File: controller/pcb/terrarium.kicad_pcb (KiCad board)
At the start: 2 copper layers, 90 x 90 mm, 57 parts, among them Q1 S8050, Q2 S8050, Q3 S8050, SW1 RESET, SW2 BOOT, SW3 RESET RTC, U1 ESP32-WROOM-32, U2 DS3231M, U3 LM1117-3.3

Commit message: pcb: refactor
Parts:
- moved R2 0.51 mm to (107.0, 75.9)
- moved R4 0.51 mm to (89.0, 75.9)
- moved R6 0.51 mm to (71.0, 75.9)
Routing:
- net +3V3: track 186.9 -> 191.3 mm, vias 4 -> 5
- net G23: track 93.7 -> 90.7 mm, vias 4 -> 2
- net Net-(D4-Pad1): track 59.5 -> 56.7 mm, vias 0 -> 2
- net SCL: track 137.3 -> 138.9 mm, vias 5 -> 3
- net SDA: track 129.5 -> 130.5 mm, vias 4 -> 2

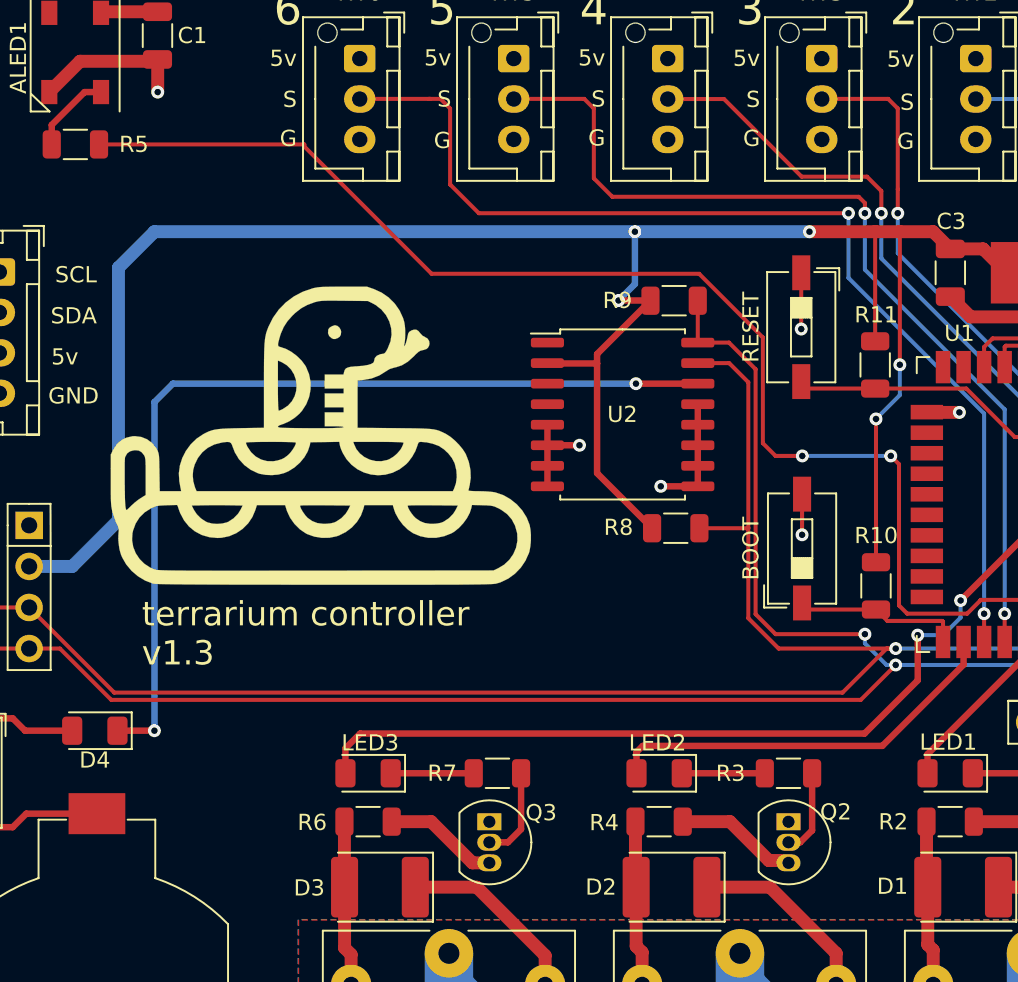
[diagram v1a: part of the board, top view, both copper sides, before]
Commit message: minor updates, bjt to sot-23
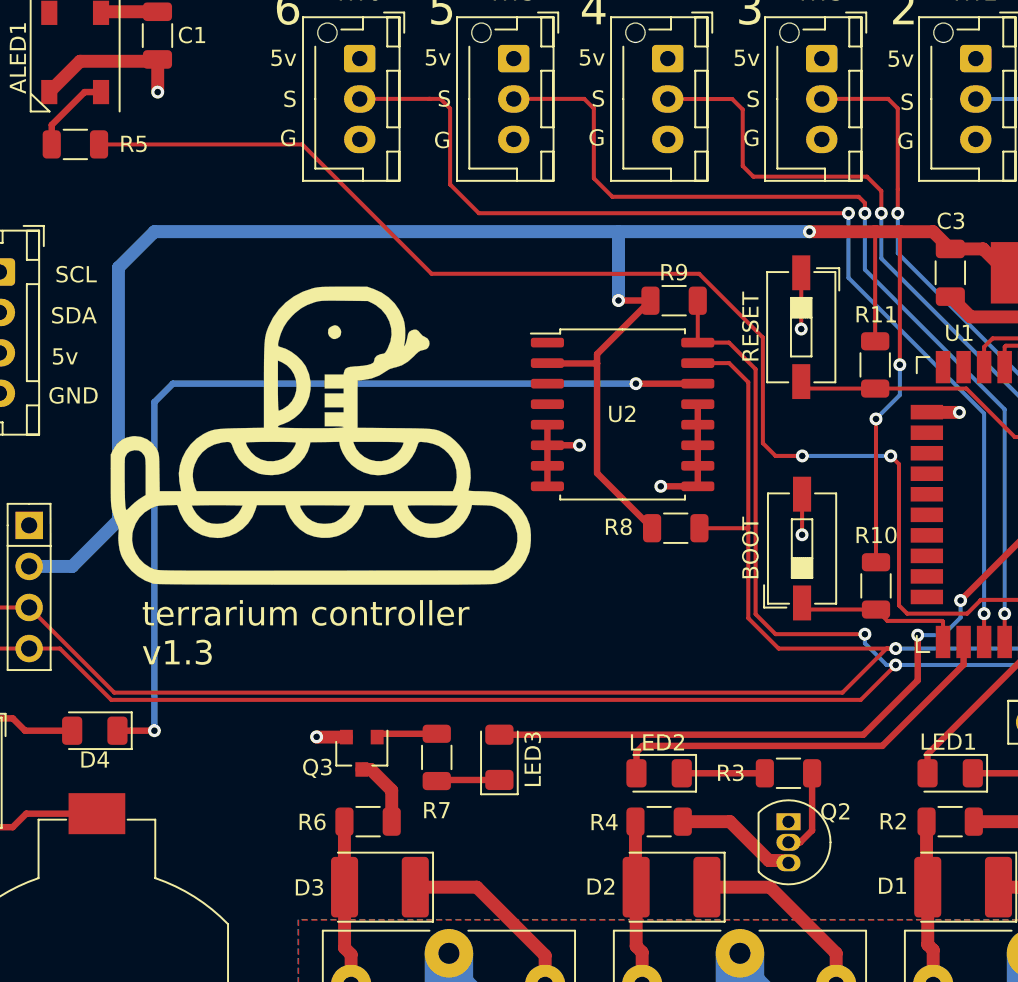
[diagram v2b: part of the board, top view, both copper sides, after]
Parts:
- Q3: footprint Package_TO_SOT_THT:TO-92_Inline -> Package_TO_SOT_SMD:SOT-23
- moved Q3 8.95 mm to (70.6, 71.6)
- moved LED3 8.18 mm to (79.1, 71.9), turned to 90 degrees
- moved R7 3.88 mm to (75.2, 71.9), turned to 90 degrees
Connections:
- Q3 pad 1: GND -> Net-(Q3-Pad1)
- Q3 pad 2: Net-(Q3-Pad2) -> GND
- R7 pad 2: Net-(Q3-Pad2) -> Net-(Q3-Pad1)
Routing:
- net G25: track 61.7 -> 50.3 mm
- net Net-(Q3-Pad2): track 5.76 -> 0.00 mm
- net Net-(Q3-Pad1): track 0.00 -> 3.77 mm
- net Net-(Q3-Pad3): track 7.26 -> 4.32 mm
- net G18: track 47.7 -> 49.7 mm
- net GND: track 79.4 -> 81.2 mm, vias 10 -> 11
- net Net-(LED3-Pad1): track 5.14 -> 3.90 mm
- net +3V3: track 191.3 -> 190.9 mm, vias 5 -> 4

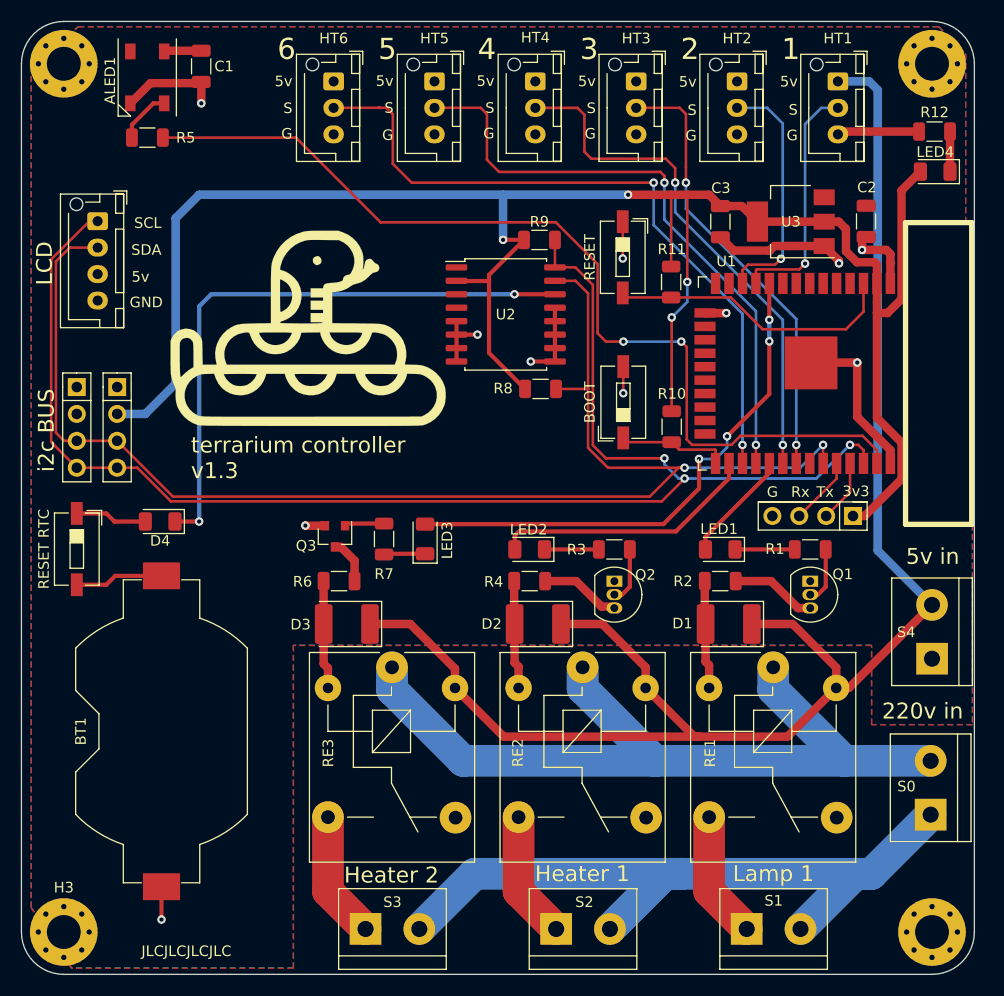
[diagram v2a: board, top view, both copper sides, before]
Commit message: rtc charge, refactoring
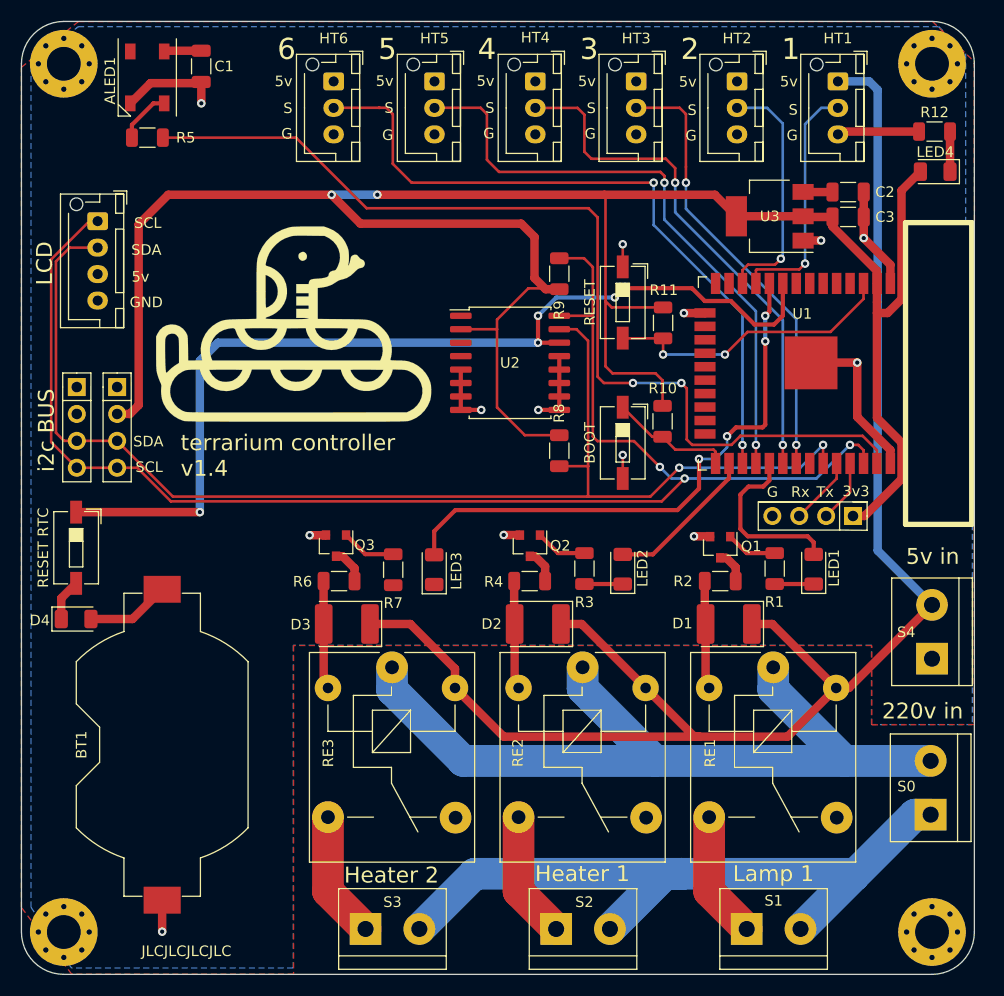
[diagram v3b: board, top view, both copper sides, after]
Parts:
- Q1, Q2: footprint Package_TO_SOT_THT:TO-92_Inline -> Package_TO_SOT_SMD:SOT-23
- moved D4 12.2 mm to (46.2, 79.4), turned to 0 degrees
- moved C3 12.1 mm to (119.1, 41.5), turned to 0 degrees
- moved Q1 9.09 mm to (107.0, 72.7)
- moved LED1 9.02 mm to (115.8, 74.7), turned to 90 degrees
- moved LED2 8.99 mm to (97.8, 74.7), turned to 90 degrees
- moved Q2 8.65 mm to (89.0, 72.5)
- moved R8 6.09 mm to (91.8, 63.5), turned to 270 degrees
- moved U2 4.59 mm to (87.1, 55.2)
- moved SW1 4.27 mm to (97.8, 49.5)
- moved R11 3.94 mm to (101.6, 51.5)
- moved SW2 3.84 mm to (97.8, 62.8), turned to 270 degrees
- moved R1 3.82 mm to (112.1, 74.7), turned to 90 degrees
- moved R9 3.70 mm to (91.8, 46.8), turned to 270 degrees
- moved R3 3.36 mm to (94.2, 74.7), turned to 90 degrees
- moved C2 3.25 mm to (119.1, 39.1), turned to 0 degrees
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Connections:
- D4 pad 2: Net-(D4-Pad2) -> Net-(BT1-Pad1)
- Q1 pad 1: GND -> Net-(Q1-Pad1)
- Q1 pad 2: Net-(Q1-Pad2) -> GND
- Q2 pad 1: GND -> Net-(Q2-Pad1)
- Q2 pad 2: Net-(Q2-Pad2) -> GND
- R1 pad 2: Net-(Q1-Pad2) -> Net-(Q1-Pad1)
- R3 pad 2: Net-(Q2-Pad2) -> Net-(Q2-Pad1)
- SW3 pad 1: Net-(D4-Pad2) -> G33
- SW3 pad 2: Net-(BT1-Pad1) -> Net-(D4-Pad1)
- U1 pad 9: Net-(U1-Pad9) -> G33
- U2 pad 14: Net-(D4-Pad1) -> G33
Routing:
- net G33: track 0.00 -> 92.2 mm, vias 0 -> 4
- net Net-(D4-Pad1): track 56.7 -> 3.95 mm, vias 2 -> 0
- net +3V3: track 190.9 -> 219.7 mm, vias 4 -> 2
- net G4: track 25.2 -> 14.4 mm
- net SDA: track 130.5 -> 120.0 mm
- net GND: track 81.2 -> 73.4 mm, vias 11 -> 13
- net Net-(D4-Pad2): track 6.79 -> 0.00 mm
- net G5: track 10.6 -> 16.7 mm
- net Net-(Q2-Pad2): track 5.30 -> 0.00 mm
- net Net-(Q1-Pad2): track 5.30 -> 0.00 mm
- net Net-(Q1-Pad3): track 8.09 -> 3.14 mm
- net Net-(Q2-Pad1): track 0.00 -> 4.90 mm
- net Net-(Q1-Pad1): track 0.00 -> 4.84 mm
- net Net-(Q2-Pad3): track 7.67 -> 3.22 mm
- net Net-(LED3-Pad1): track 3.90 -> 0.00 mm
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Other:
- board text added: "terrarium controller v1.4"
- board text added: "terrarium controller v1.4 github.com/brushknight/terrarium github.com/brushknight/terrarium-hardware"
- board text removed: "terrarium controller v1.3"
- board text removed: "terrarium controller v1.3 github.com/brushknight/terrarium github.com/brushknight/terrarium-hardware"

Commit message: update jst footprints, added missing 3d models
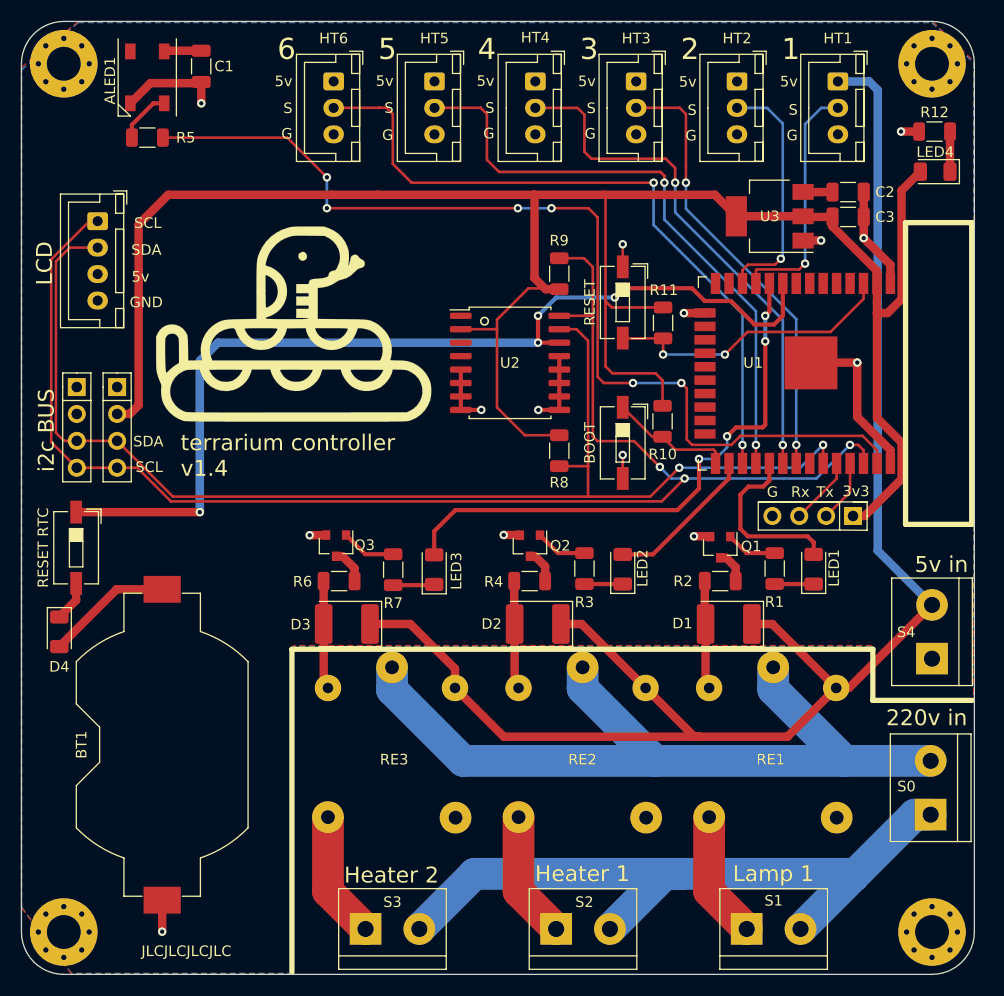
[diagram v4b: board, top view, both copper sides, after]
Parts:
- moved D4 1.99 mm to (44.6, 80.6), turned to 270 degrees
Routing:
- net +3V3: track 219.7 -> 202.9 mm, vias 2 -> 0
- net GND: track 73.4 -> 67.7 mm, vias 13 -> 14
- net Net-(BT1-Pad1): track 7.89 -> 12.0 mm
- net Net-(LED3-Pad1): track 0.00 -> 3.90 mm
- net G23: track 93.3 -> 95.0 mm, vias 2 -> 6

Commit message: refactoring
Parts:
- moved R7 7.32 mm to (81.6, 79.7), turned to 180 degrees
- moved R1 7.28 mm to (117.5, 79.6), turned to 180 degrees
- moved R3 7.19 mm to (99.4, 79.6), turned to 180 degrees
- moved Q3 6.47 mm to (76.4, 75.6), turned to 180 degrees
- moved Q2 6.32 mm to (94.5, 75.7), turned to 180 degrees
- moved Q1 6.29 mm to (112.5, 75.7), turned to 180 degrees
- moved G*** 2.33 mm to (67.4, 53.8)
- moved LED1 2.11 mm to (117.6, 75.9), turned to 180 degrees
- moved LED2 2.10 mm to (99.5, 75.9), turned to 180 degrees
- moved LED3 1.88 mm to (81.6, 75.8), turned to 180 degrees
- moved R6 0.24 mm to (71.1, 75.6)
- moved R4 0.17 mm to (89.0, 75.7)
- moved R2 0.17 mm to (107.0, 75.7)
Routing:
- net +5V: track 153.3 -> 278.9 mm
- net GND: track 67.7 -> 60.2 mm
- net G4: track 14.4 -> 19.1 mm
- net SCL: track 139.6 -> 143.6 mm
- net G25: track 53.4 -> 57.0 mm
- net G5: track 16.7 -> 19.2 mm
- net G33: track 92.2 -> 93.4 mm, vias 4 -> 3
- net Net-(Q3-Pad3): track 3.43 -> 2.89 mm
- removed copper zone on F.Cu, net +5V
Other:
- board text added: "terrarium controller"
- board text added: "v1.4"
- board text removed: "terrarium controller v1.4"

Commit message: minor changes
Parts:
- D1, D2, D3: footprint Diode_SMD:D_2114_3652Metric -> Diode_SMD:D_2010_5025Metric
- moved R8 4.04 mm to (88.0, 62.1), turned to 0 degrees
- moved R9 3.96 mm to (88.1, 48.1), turned to 180 degrees
- moved C3 3.55 mm to (120.3, 44.8), turned to 180 degrees
- moved C2 1.27 mm to (120.3, 39.1), turned to 180 degrees
- moved D3 0.09 mm to (71.8, 79.9)
- moved D2 0.06 mm to (89.8, 79.9)
- moved D1 0.06 mm to (107.9, 79.9)
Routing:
- net GND: track 60.2 -> 42.1 mm, vias 14 -> 17
- net +3V3: track 202.9 -> 185.2 mm
- net +5V: track 278.9 -> 293.6 mm
- net G33: track 93.4 -> 83.3 mm, vias 3 -> 5
- net SCL: track 143.6 -> 139.9 mm, vias 3 -> 2
- net Net-(R11-Pad2): track 27.9 -> 26.9 mm
- net G25: track 57.0 -> 56.2 mm

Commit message: diode for battery
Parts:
- D4: footprint Diode_SMD:D_1206_3216Metric -> Diode_SMD:D_2010_5025Metric
- moved D4 12.6 mm to (54.2, 72.5), turned to 0 degrees
- moved G*** 1.89 mm to (66.8, 52.0)
- moved R5 0.12 mm to (53.0, 34.0), turned to 0 degrees
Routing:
- net Net-(BT1-Pad1): track 12.0 -> 5.02 mm
- net G23: track 94.7 -> 99.3 mm
- net Net-(D4-Pad1): track 3.83 -> 7.29 mm
- net Net-(ALED1-Pad4): track 5.10 -> 3.24 mm

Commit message: fix bugs in UART
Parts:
- removed R10: 10k, Resistor_SMD:R_1206_3216Metric
- removed SW2: BOOT, Button_Switch_SMD:SW_DIP_SPSTx01_Slide_6.7x4.1mm_W6.73mm_P2.54mm_LowProfile_JPin
- added RESET_j1: data, Connector_PinHeader_2.54mm:PinHeader_1x02_P2.54mm_Vertical, F.Cu at (98.7, 56.1)
- added TP1: TestPoint, TestPoint:TestPoint_Pad_1.5x1.5mm, F.Cu at (101.2, 59.5)
- added TP2: TestPoint, TestPoint:TestPoint_Pad_1.5x1.5mm, F.Cu at (98.7, 59.5)
- UART1: footprint Connector_PinHeader_2.54mm:PinHeader_1x04_P2.54mm_Vertical -> Connector_PinHeader_2.54mm:PinHeader_1x06_P2.54mm_Vertical
- moved HT3 5.59 mm to (93.5, 28.7)
- moved HT5 5.59 mm to (74.4, 28.7)
- moved HT1 5.59 mm to (112.5, 28.7)
- moved HT2 5.59 mm to (103.0, 28.7)
- moved HT4 5.59 mm to (83.9, 28.7)
- moved HT6 5.59 mm to (64.9, 28.7)
- moved UART1 2.49 mm to (121.9, 70.6)
- moved D1 0.38 mm to (107.9, 79.5)
- moved D2 0.38 mm to (89.8, 79.5)
- moved D3 0.38 mm to (71.8, 79.5)
- turned C2 to 0 degrees
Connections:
- U1 pad 25: Net-(R10-Pad2) -> IO0
- U1 pad 3: Net-(R11-Pad2) -> EN
- UART1 pad 1: +3V3 -> GND
- UART1 pad 2: TX -> +3V3
- UART1 pad 3: RX -> TX
- UART1 pad 4: GND -> RX
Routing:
- net EN: track 0.00 -> 60.3 mm, vias 0 -> 3
- net +5V: track 293.6 -> 332.5 mm, vias 0 -> 1
- net +3V3: track 185.2 -> 168.9 mm
- net Net-(R11-Pad2): track 26.9 -> 12.2 mm, vias 2 -> 0
- net IO0: track 0.00 -> 14.6 mm, vias 0 -> 2
- net Net-(R10-Pad2): track 11.6 -> 0.00 mm
- net G16: track 66.0 -> 71.9 mm
- net G17: track 57.6 -> 63.3 mm
- net G18: track 49.7 -> 55.3 mm
- net G19: track 42.7 -> 46.6 mm
- net G4: track 19.1 -> 15.2 mm
- net SDA: track 120.2 -> 123.2 mm
- net G5: track 19.2 -> 22.2 mm
- net G33: track 83.3 -> 86.2 mm
- net G27: track 24.6 -> 27.0 mm
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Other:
- board text added: "En"
- board text added: "Gnd"
- board text added: "IO0"
